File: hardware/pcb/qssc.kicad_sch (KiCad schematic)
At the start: 124 parts, among them J1 FT232RL, J10 USB-C, J12 BTB_HOST, J2 5V Barrel, J3 SMA, J4 12V LED, J7 RESET, J8 MW_GATE, J9 JTAG, U1 XC7A35T-1CSG324C, U3 ADF4351BCPZ, U5 GVA-84+, U8 W25Q128JVSIQ, Y1 100MHz TCXO

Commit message: pcb: Ironwood SBT socket + per-datasheet pin fixes + no_connect markers
Step 0 — Ironwood SBT open-top spring-pin socket (emitter face, main board):
  - socket_footprint(): 65 solder pads (64 EM + EM_ANODE) on F.Cu+F.Paste+F.Mask
    at the 0.30mm die-contact pitch, 4 NPTH M2 mount holes, 25x25mm body +
    courtyard. lib_id "qssc:Ironwood_SBT" + symbol; Uchip swapped from
    QSSC_Chip_EM. This is the commercial made-to-order socket that fits the
    20x20mm / 0.30mm-pitch die (no off-the-shelf socket exists at that pitch).
  - Head-board QSSC_Chip_DET (detector face) unchanged: ACF/pogo on B.Cu.

Step 1 — per-datasheet pin audit + (no_connect) emission (addresses
"practically nothing connected per its datasheet"):
  - FT232RL: net pin 24 -> +3V3 (VCC) and pin 23 -> GND (AGND) -- both required
    supply/ground pads per SSOP-28 that were previously unnetted.
  - ADF4351: REFIN- (pin 19) decoupled to GND via new C37 100nF (single-ended
    CMOS ref, datasheet Fig.51); unused RFOUTB+/- (13,14), RFOUTA- (15), SW (5),
    CE (25) declared no_connect per datasheet (unused RF outputs float).
  - add() now takes nc_pins=...; emit_schematic() emits (no_connect) sexps at
    every documented-unused pin: FT232 modem/crystal/LED (12 pins), ADF4351 (5),
    AD7616 parallel-DB bus + SDI/SDOB in 1-wire HW mode (10/chip x4 = 40 head),
    TLC5947 chip2 OUT16-23 + SOUT (9 main).

Both boards: DRC 0/0/0, ERC 0 errors / 0 warnings. 9 PCB tests green.

Co-Authored-By: Claude Code <noreply@anthropic.com>
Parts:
- removed Uchip: QSSC_Chip_EM, qssc:QSSC_Chip_EM, symbol qssc:QSSC_Chip_EM
- added C37: 100n, Capacitor_SMD:C_0603_1608Metric, symbol qssc:C
- added Uchip: Ironwood_SBT, qssc:Ironwood_SBT, symbol qssc:Ironwood_SBT
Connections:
- net +12V_EMIT: now also Uchip.EM_ANODE
- net GND: now also J1.23 (CBUS0), C37.2
- net emitter_cat0: now also Uchip.EM0
- net emitter_cat1: now also Uchip.EM1
- net emitter_cat10: now also Uchip.EM10
- net emitter_cat11: now also Uchip.EM11
- net emitter_cat12: now also Uchip.EM12
- net emitter_cat13: now also Uchip.EM13
- net emitter_cat14: now also Uchip.EM14
- net emitter_cat15: now also Uchip.EM15
- net emitter_cat16: now also Uchip.EM16
- net emitter_cat17: now also Uchip.EM17
- net emitter_cat18: now also Uchip.EM18
- net emitter_cat19: now also Uchip.EM19
- net emitter_cat2: now also Uchip.EM2
- net emitter_cat20: now also Uchip.EM20
- net emitter_cat21: now also Uchip.EM21
- net emitter_cat22: now also Uchip.EM22
- net emitter_cat23: now also Uchip.EM23
- net emitter_cat24: now also Uchip.EM24
- net emitter_cat25: now also Uchip.EM25
- net emitter_cat26: now also Uchip.EM26
- net emitter_cat27: now also Uchip.EM27
- net emitter_cat28: now also Uchip.EM28
- net emitter_cat29: now also Uchip.EM29
- net emitter_cat3: now also Uchip.EM3
- net emitter_cat30: now also Uchip.EM30
- net emitter_cat31: now also Uchip.EM31
- net emitter_cat32: now also Uchip.EM32
- net emitter_cat33: now also Uchip.EM33
- net emitter_cat34: now also Uchip.EM34
- net emitter_cat35: now also Uchip.EM35
- net emitter_cat36: now also Uchip.EM36
- net emitter_cat37: now also Uchip.EM37
- net emitter_cat38: now also Uchip.EM38
- net emitter_cat39: now also Uchip.EM39
- net emitter_cat4: now also Uchip.EM4
- net emitter_cat40: now also Uchip.EM40
- net emitter_cat41: now also Uchip.EM41
- net emitter_cat42: now also Uchip.EM42
- net emitter_cat43: now also Uchip.EM43
- net emitter_cat44: now also Uchip.EM44
- net emitter_cat45: now also Uchip.EM45
- net emitter_cat46: now also Uchip.EM46
- net emitter_cat47: now also Uchip.EM47
- net emitter_cat48: now also Uchip.EM48
- net emitter_cat49: now also Uchip.EM49
- net emitter_cat5: now also Uchip.EM5
- net emitter_cat50: now also Uchip.EM50
- net emitter_cat51: now also Uchip.EM51
- net emitter_cat52: now also Uchip.EM52
- net emitter_cat53: now also Uchip.EM53
- net emitter_cat54: now also Uchip.EM54
- net emitter_cat55: now also Uchip.EM55
- net emitter_cat56: now also Uchip.EM56
- net emitter_cat57: now also Uchip.EM57
- net emitter_cat58: now also Uchip.EM58
- net emitter_cat59: now also Uchip.EM59
- net emitter_cat6: now also Uchip.EM6
- net emitter_cat60: now also Uchip.EM60
- net emitter_cat61: now also Uchip.EM61
- net emitter_cat62: now also Uchip.EM62
- net emitter_cat63: now also Uchip.EM63
- net emitter_cat7: now also Uchip.EM7
- net emitter_cat8: now also Uchip.EM8
- net emitter_cat9: now also Uchip.EM9
- net REFIN_N: now reaches U3.19 (TEMP)
- net REFIN_N: now also C37.1
- no-connect marks 0 -> 26
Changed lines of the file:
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@@
 	(symbol
 		(lib_id "qssc:C")
+		(at 315 185 0)
+		(unit 1)
+		(exclude_from_sim no)
+		(in_bom yes)
+		(on_board yes)
+		(dnp no)
+		(property "Reference" "C37"
+			(at 315 183 0)
+			(effects
+				(font
+					(size 1.27 1.27)
+				)
+			)
+		)
+		(property "Value" "100n"
+			(at 315 187 0)
+			(effects
+				(font
+					(size 1.27 1.27)
+				)
+			)
+		)
+		(property "Footprint" "Capacitor_SMD:C_0603_1608Metric"
+			(at 315 185 0)
+			(effects
+				(font
+					(size 1.27 1.27)
+				)
+				(hide yes)
+			)
+		)
+		(pin "1"
+		)
+		(pin "2"
+		)
+		(instances
+			(project "qssc"
+				(path "/00000000-0000-0000-0000-000000000001"
+					(reference "C37")
+					(unit 1)
+				)
+			)
+		)
+	)
+	(symbol
+		(lib_id "qssc:C")
 		(at 330 150 0)
 		(unit 1)
@@
 	)
 	(symbol
-		(lib_id "qssc:QSSC_Chip_EM")
+		(lib_id "qssc:Ironwood_SBT")
 		(at 80 55 0)
 		(unit 1)
@@
 			)
 		)
-		(property "Value" "QSSC_Chip_EM"
+		(property "Value" "Ironwood_SBT"
 			(at 80 57 0)
 			(effects
@@
 			)
 		)
-		(property "Footprint" "qssc:QSSC_Chip_EM"
+		(property "Footprint" "qssc:Ironwood_SBT"
 			(at 80 55 0)
 			(effects
@@
 	)
 	(label "GND"
+		(at 289.84 75.08 0)
+		(fields_autoplaced yes)
+		(effects
+			(font
+				(size 1.27 1.27)
+			)
+			(justify left bottom)
+		)
+	)
+	(label "GND"
 		(at 303.81 62.38 0)
 		(fields_autoplaced yes)
@@
 		)
 	)
+	(label "REFIN_N"
+		(at 289.84 136.03 0)
+		(fields_autoplaced yes)
+		(effects
+			(font
+				(size 1.27 1.27)
+			)
+			(justify left bottom)
+		)
+	)
 	(label "LF_CP"
 		(at 250.0 171.19 0)
@@
 		)
 	)
+	(label "REFIN_N"
+		(at 315.0 181.19 0)
+		(fields_autoplaced yes)
+		(effects
+			(font
+				(size 1.27 1.27)
+			)
+			(justify left bottom)
+		)
+	)
+	(label "GND"
+		(at 315.0 188.81 0)
+		(fields_autoplaced yes)
+		(effects
+			(font
+				(size 1.27 1.27)
+			)
+			(justify left bottom)
+		)
+	)
 	(label "RF_OUT"
 		(at 330.0 146.19 0)
@@
 		)
 	)
+	(no_connect
+		(at 310.16 68.73)
+	)
+	(no_connect
+		(at 310.16 73.81)
+	)
+	(no_connect
+		(at 289.84 85.24)
+	)
+	(no_connect
+		(at 289.84 87.78)
+	)
+	(no_connect
+		(at 289.84 52.22)
+	)
+	(no_connect
+		(at 289.84 54.76)
+	)
+	(no_connect
+		(at 289.84 57.3)
+	)
+	(no_connect
+		(at 289.84 59.84)
+	)
+	(no_connect
+		(at 289.84 62.38)
+	)
+	(no_connect
+		(at 289.84 72.54)
+	)
+	(no_connect
+		(at 289.84 80.16)
+	)
+	(no_connect
+		(at 310.16 71.27)
+	)
+	(no_connect
+		(at 289.84 163.97)
+	)
+	(no_connect
+		(at 310.16 147.46)
+	)
+	(no_connect
+		(at 310.16 150.0)
+	)
+	(no_connect
+		(at 310.16 152.54)
+	)
+	(no_connect
+		(at 289.84 151.27)
+	)
+	(no_connect
+		(at 562.16 31.43)
+	)
+	(no_connect
+		(at 562.16 33.97)
+	)
+	(no_connect
+		(at 562.16 36.51)
+	)
+	(no_connect
+		(at 562.16 39.05)
+	)
+	(no_connect
+		(at 562.16 41.59)
+	)
+	(no_connect
+		(at 562.16 44.13)
+	)
+	(no_connect
+		(at 562.16 46.67)
+	)
+	(no_connect
+		(at 562.16 49.21)
+	)
+	(no_connect
+		(at 541.84 18.73)
+	)
 	(sheet_instances

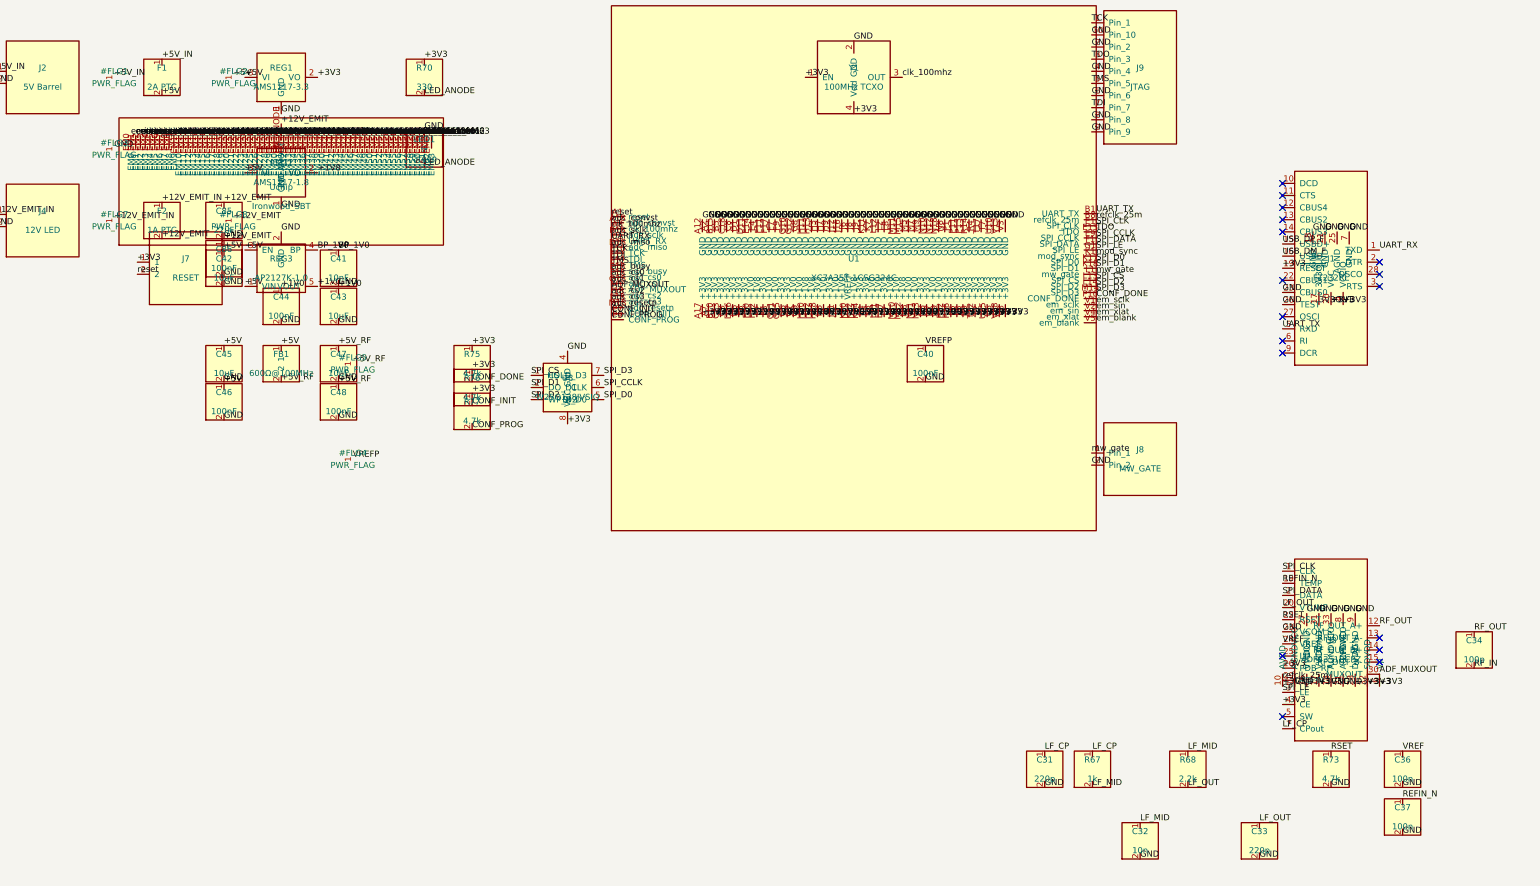
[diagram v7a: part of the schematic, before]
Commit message: pcb: verify netlist complete per datasheets, fix C_in/C37 placement short
Connection audit (tools/audit_connections.py) confirms both boards are
netlist-complete and datasheet-correct BEFORE routing:

  - ERC: 0 errors both boards (qssc + chip_module). The 145/203 remaining
    messages are all endpoint_off_grid warnings (authored symbols on a
    non-1.27 mm pin grid) -- cosmetic noise.
  - DRC: 0 violations, 0 unconnected pads, 0 footprint errors both boards.
  - Chip die: 64 emitter_cat -> TLC5947 OUT sinks + EM_ANODE -> +12V_EMIT
    on the main board; 64 DET_IN -> TLV9004 TIA -> AD7616 + DET_REF on the
    head. Every chip net has an off-chip destination (audit confirms).
  - All 268 main-board + head "unnetted" IC pins are intentional spares,
    not missing connections: FPGA 185 spare IO balls (99 power balls all
    netted), AD7616 parallel-DB bus + SDI/SDOB in 1-wire HW serial mode,
    FT232 modem/CBUS pins (USB-only; pin 23 AGND + 24 VCC ARE netted),
    ADF4351 NC pins 5/13/14/15/25 per datasheet, TLC5947 chip2 unused
    OUT16-23 + SOUT, and numberless EP/mount-hole cosmetic pads.

Fix: the main board had 3 DRC violations (shorting_items +5V_IN/ADF_TEMP,
courtyards_overlap, solder_mask_bridge) all from ONE root cause -- the new
input-bulk cap C_in and the ADF4351 TEMP decoupler C37 both fell through
assign_pcb_positions()'s else-branch to the (50,50) default cell, so
C_in.1 (+5V_IN) overlapped C37.1 (ADF_TEMP). Give both explicit placements
in the fixed dict (C_in @46,8 near the barrel jack; C37 @104,36 below U3).
Regenerated both boards -> DRC 0/0/0.

route_signals.py: the chip-net force-fail referenced an undefined
`structured_chip` (NameError if run). Define it as an empty set so the
file is runnable and all chip nets are cleanly deferred to the future
_structured_bus_fanout (task #36) / FreeRouting -- routing stays paused
per the user's instruction until the netlist was verified.

Adds tools/audit_connections.py (per-datasheet pin/rail/chip audit) a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
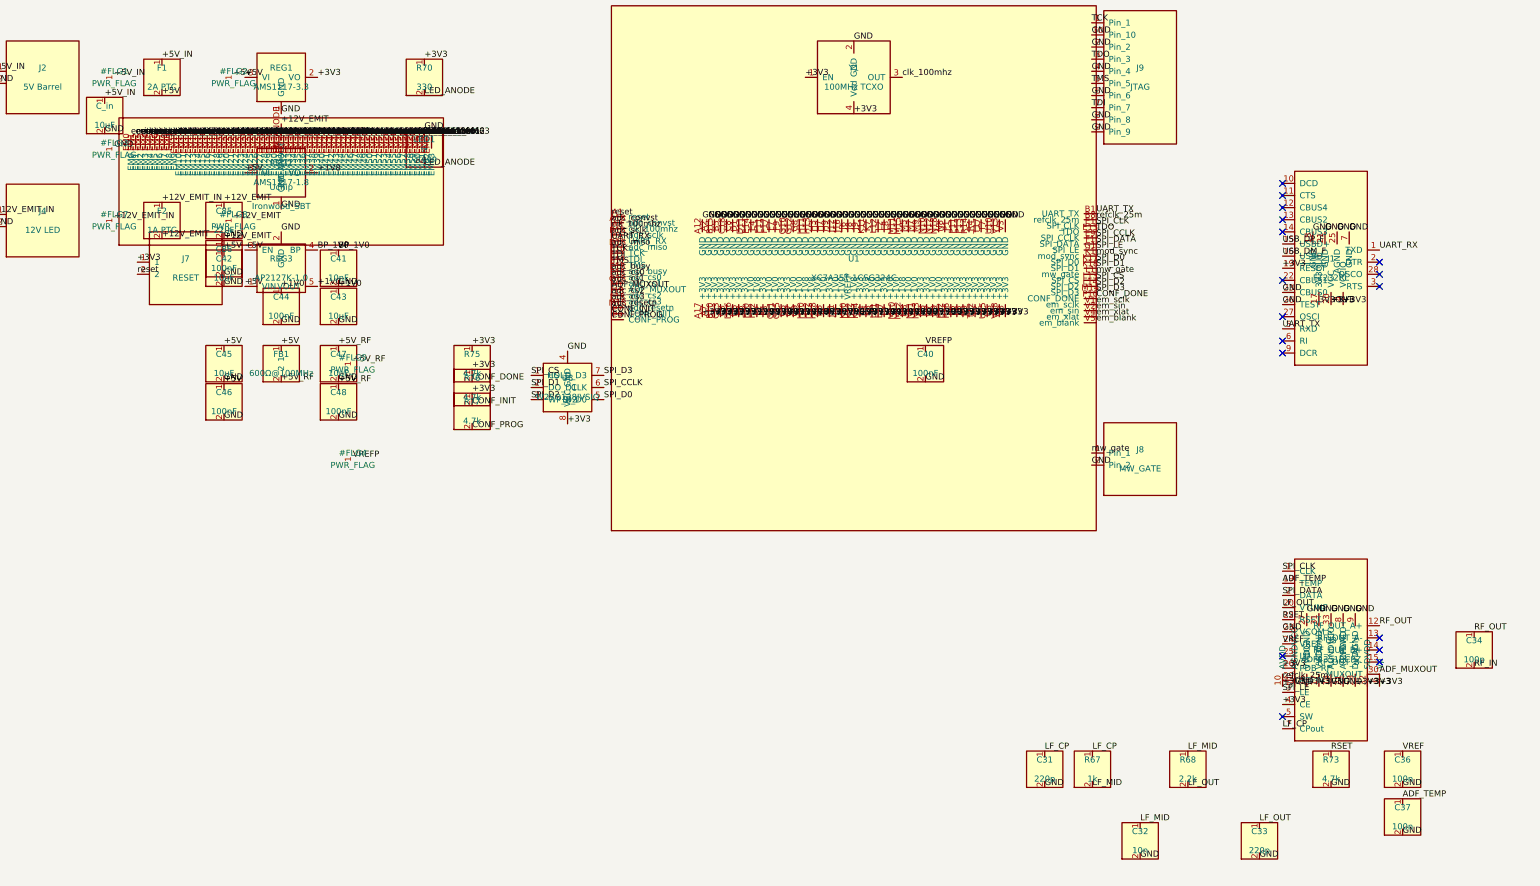
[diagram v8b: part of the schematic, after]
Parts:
- added C_in: 10uF, Capacitor_SMD:C_0805_2012Metric, symbol qssc:C
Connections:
- net +5V_IN: now also C_in.1
- net GND: now also C_in.2
- net REFIN_N renamed ADF_TEMP
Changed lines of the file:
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@@
 	)
 	(symbol
+		(lib_id "qssc:C")
+		(at 43 38 0)
+		(unit 1)
+		(exclude_from_sim no)
+		(in_bom yes)
+		(on_board yes)
+		(dnp no)
+		(property "Reference" "C_in"
+			(at 43 36 0)
+			(effects
+				(font
+					(size 1.27 1.27)
+				)
+			)
+		)
+		(property "Value" "10uF"
+			(at 43 40 0)
+			(effects
+				(font
+					(size 1.27 1.27)
+				)
+			)
+		)
+		(property "Footprint" "Capacitor_SMD:C_0805_2012Metric"
+			(at 43 38 0)
+			(effects
+				(font
+					(size 1.27 1.27)
+				)
+				(hide yes)
+			)
+		)
+		(pin "1"
+		)
+		(pin "2"
+		)
+		(instances
+			(project "qssc"
+				(path "/00000000-0000-0000-0000-000000000001"
+					(reference "C_in")
+					(unit 1)
+				)
+			)
+		)
+	)
+	(symbol
 		(lib_id "qssc:Polyfuse")
 		(at 55 30 0)
@@
 	)
 	(label "+5V_IN"
+		(at 43.0 34.19 0)
+		(fields_autoplaced yes)
+		(effects
+			(font
+				(size 1.27 1.27)
+			)
+			(justify left bottom)
+		)
+	)
+	(label "GND"
+		(at 43.0 41.81 0)
+		(fields_autoplaced yes)
+		(effects
+			(font
+				(size 1.27 1.27)
+			)
+			(justify left bottom)
+		)
+	)
+	(label "+5V_IN"
 		(at 55.0 26.19 0)
 		(fields_autoplaced yes)
@@
 		)
 	)
-	(label "REFIN_N"
+	(label "ADF_TEMP"
 		(at 289.84 136.03 0)
 		(fields_autoplaced yes)
@@
 		)
 	)
-	(label "REFIN_N"
+	(label "ADF_TEMP"
 		(at 315.0 181.19 0)
 		(fields_autoplaced yes)
